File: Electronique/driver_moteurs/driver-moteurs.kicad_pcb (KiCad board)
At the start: 2 copper layers, 51 parts, among them P1 CONN_ENCODER, P2 CONN_02_FREE, P3 CONN_I2C, P4 CONN_Servo, P5 CONN_FC, P6 CONN_SERIAL, P7 CONN_SWDIO, P8 CONN_CAN, U1 stm32f303k8t6, U10 Trou-3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

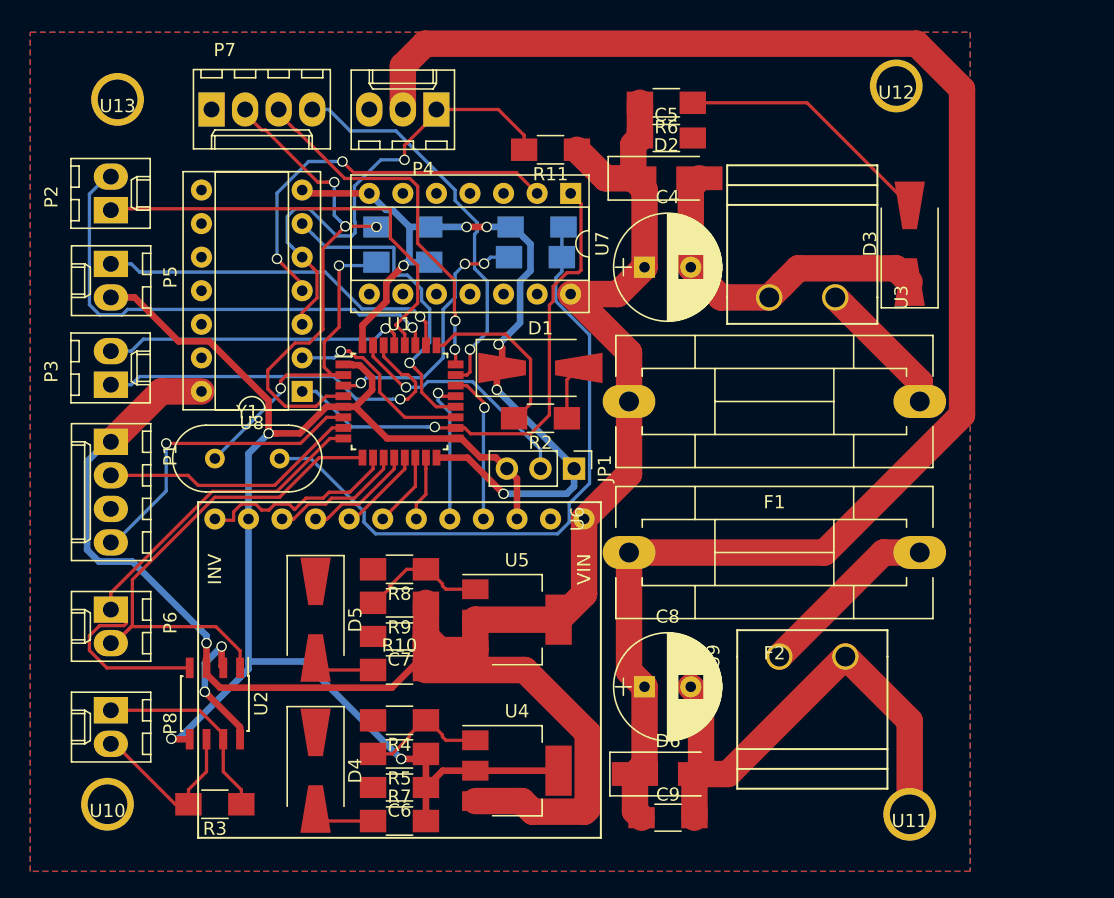
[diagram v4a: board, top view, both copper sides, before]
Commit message: Correction PCB driver moteurs
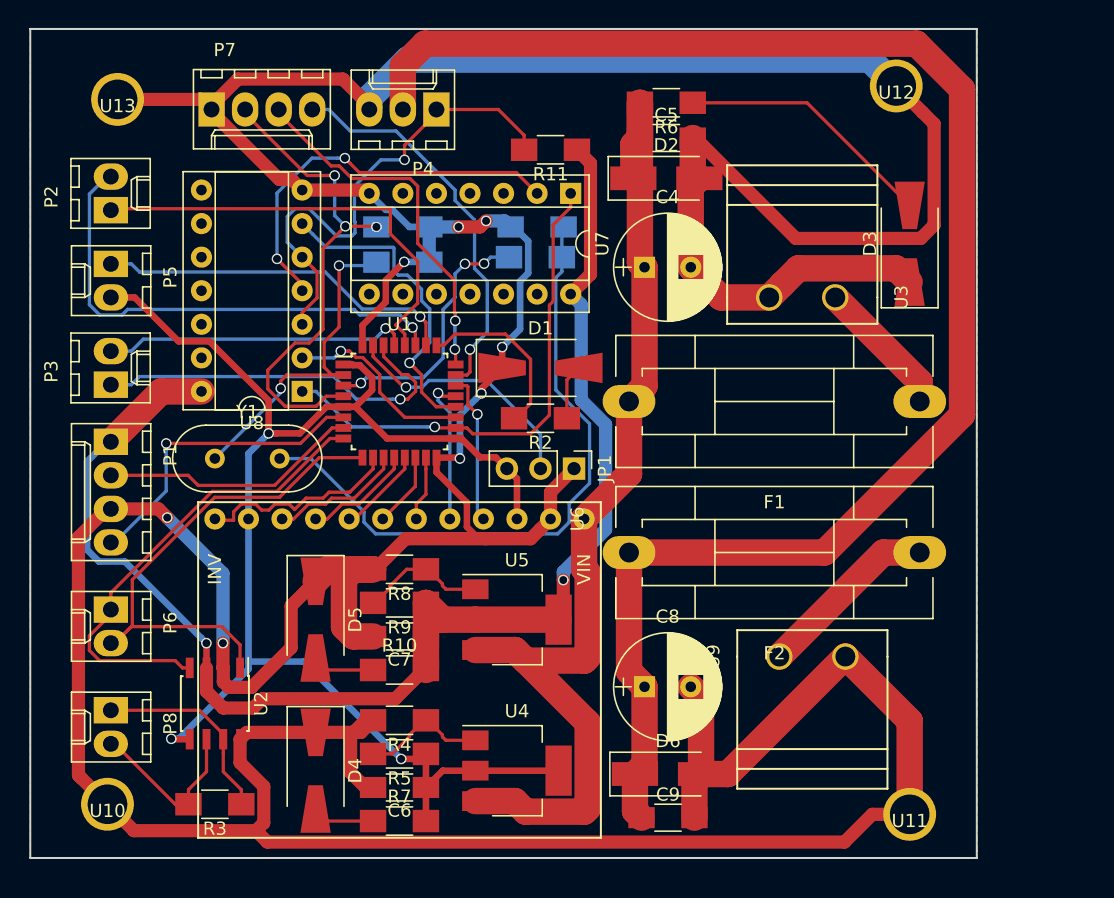
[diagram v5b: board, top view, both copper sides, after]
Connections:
- C4 pad 1: +5V -> VDD
- C5 pad 1: +5V -> VDD
- D2 pad 1: +5V -> VDD
- F1 pad 2: +5V -> VDD
- R6 pad 2: +5V -> VDD
- U4 pad 3: +5V -> VDD
- U5 pad 3: +5V -> VDD
- U6 pad 1: +5V -> VDD
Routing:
- net GND: track 140.7 -> 414.3 mm
- net VDD: track 0.00 -> 82.2 mm
- net +5V: track 151.5 -> 106.8 mm, vias 1 -> 2
- net /TX: track 38.2 -> 35.6 mm
- net /EN_Servo: track 39.2 -> 38.1 mm
- net Net-(JP1-Pad2): track 18.2 -> 19.0 mm
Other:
- board outline added: 71.6 x 62.7 mm

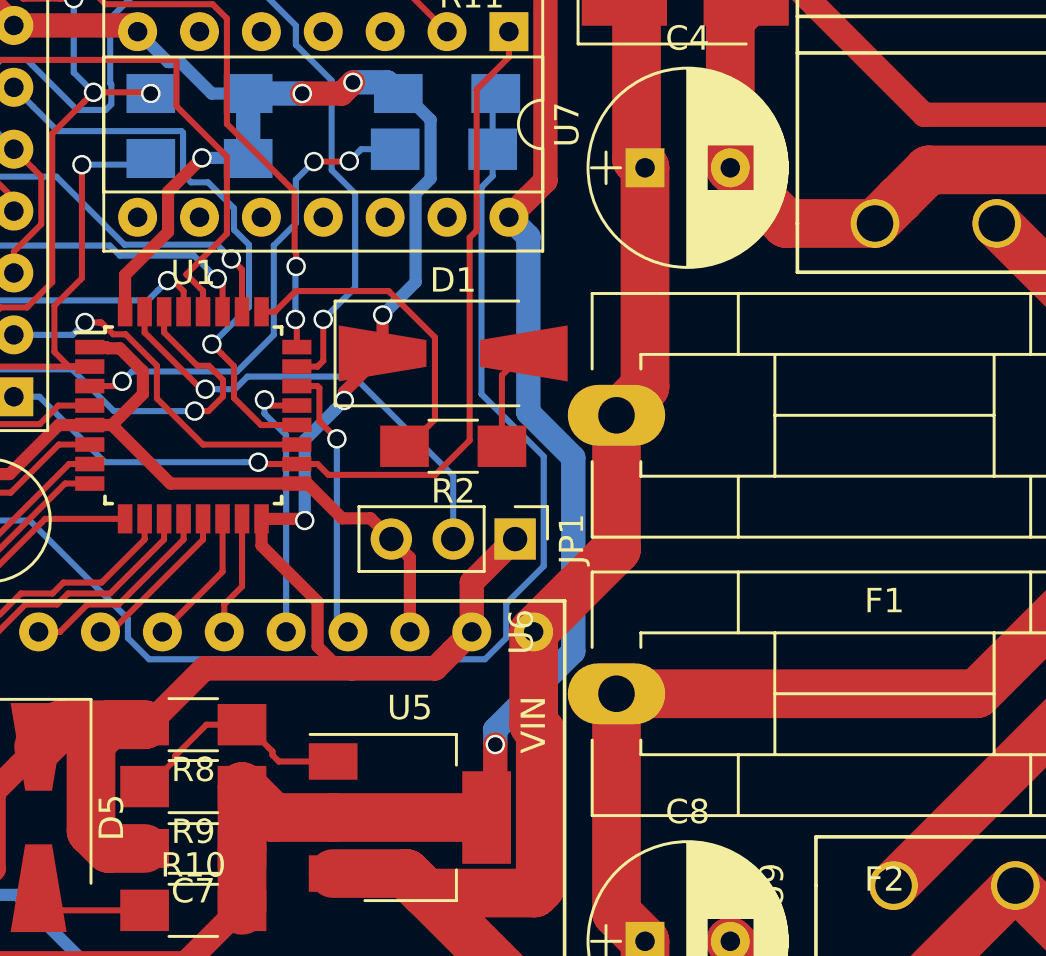
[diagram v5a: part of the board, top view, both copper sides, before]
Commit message: GND driver moteur
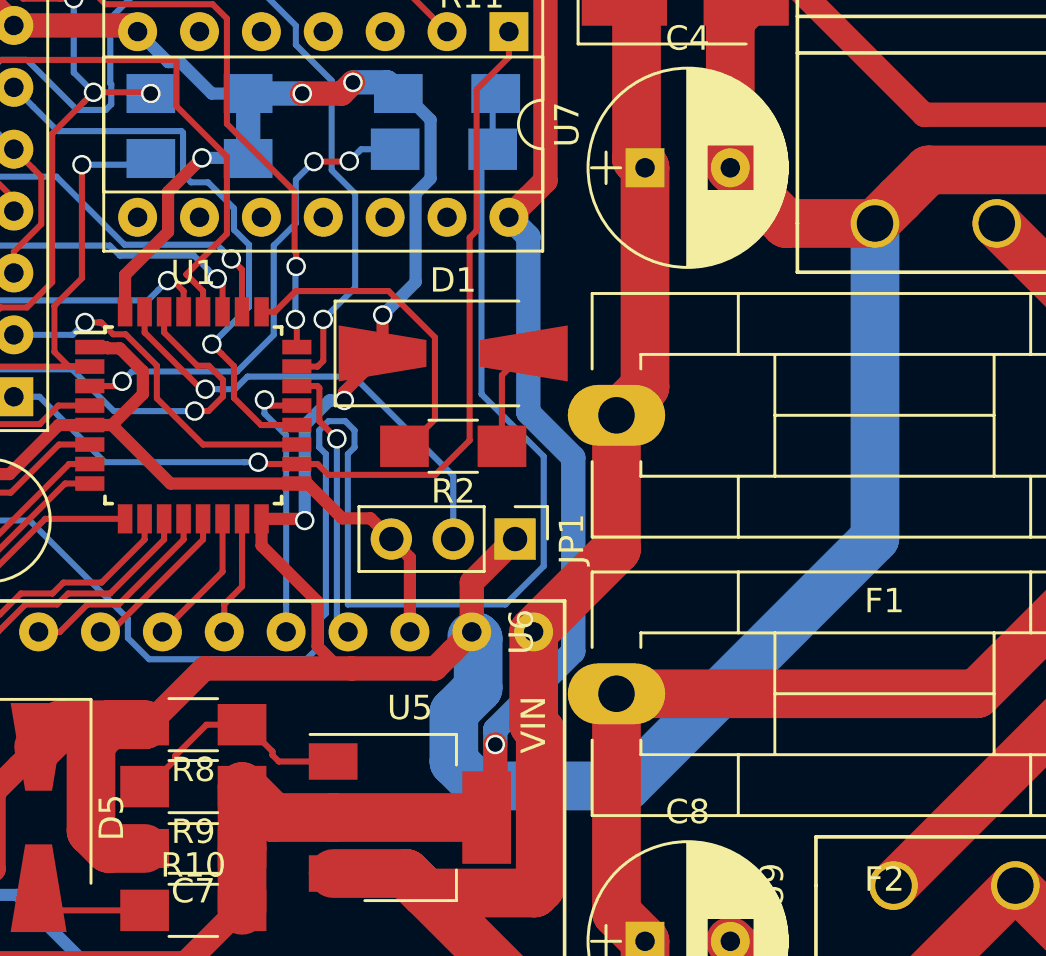
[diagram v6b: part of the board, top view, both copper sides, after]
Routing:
- net GND: track 414.3 -> 455.5 mm
- net Net-(C2-Pad1): track 49.4 -> 64.8 mm
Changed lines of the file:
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@@
     (links 117)
     (no_connects 0)
-    (area 0 0 0 0)
+    (area 92.634999 70.783998 164.420012 133.785)
     (thickness 1.6)
     (drawings 5)
-    (tracks 655)
+    (tracks 676)
     (zones 0)
     (modules 51)
@@
   )
   (setup
-    (last_trace_width 0.25)
+    (last_trace_width 2)
     (user_trace_width 0.25)
     (user_trace_width 0.5)
@@
   (segment (start 111.662629 97.502435) (end 111.662629 98.06812) (width 0.25) (layer F.Cu) (net 1))
   (via (at 111.662629 98.06812) (size 0.8) (drill 0.6) (layers F.Cu B.Cu) (net 1))
-  (segment (start 126.447601 98.850399) (end 126.8476 98.4504) (width 0.5) (layer B.Cu) (net 2))
-  (segment (start 125.222 100.076) (end 126.447601 98.850399) (width 0.5) (layer B.Cu) (net 2))
-  (segment (start 125.222 103.378) (end 125.222 100.076) (width 0.5) (layer B.Cu) (net 2))
+  (segment (start 126.281915 98.4504) (end 126.8476 98.4504) (width 0.5) (layer B.Cu) (net 2))
+  (segment (start 126.23141 98.4504) (end 126.281915 98.4504) (width 0.5) (layer B.Cu) (net 2))
+  (segment (start 131.34519 113.276967) (end 131.34519 111.252903) (width 2) (layer B.Cu) (net 2))
+  (segment (start 125.222 99.45981) (end 126.23141 98.4504) (width 0.5) (layer B.Cu) (net 2))
+  (segment (start 125.222 103.378) (end 125.222 99.45981) (width 0.5) (layer B.Cu) (net 2))
+  (segment (start 132.341033 114.27281) (end 131.34519 113.276967) (width 2) (layer B.Cu) (net 2))
+  (segment (start 131.34519 111.252903) (end 132.341033 110.25706) (width 2) (layer B.Cu) (net 2))
+  (segment (start 132.341033 110.25706) (end 132.341033 108.211033) (width 2) (layer B.Cu) (net 2))
+  (segment (start 132.341033 108.211033) (end 132.280009 108.150009) (width 2) (layer B.Cu) (net 2))
+  (segment (start 132.280009 108.150009) (end 132.08 108.150009) (width 2) (layer B.Cu) (net 2))
+  (segment (start 148.63 91.186) (end 148.63 104.094837) (width 2) (layer B.Cu) (net 2))
+  (segment (start 148.63 104.094837) (end 138.452027 114.27281) (width 2) (layer B.Cu) (net 2))
+  (segment (start 138.452027 114.27281) (end 132.341033 114.27281) (width 2) (layer B.Cu) (net 2))
+  (segment (start 132.341033 114.27281) (end 132.165023 114.0968) (width 2) (layer B.Cu) (net 2))
   (segment (start 118.364 76.962) (end 118.364 76.090717) (width 2) (layer B.Cu) (net 2))
   (segment (start 118.364 76.090717) (end 121.270716 73.184001) (width 2) (layer B.Cu) (net 2))
@@
   (segment (start 142.97 130.556) (end 142.97 127.754) (width 2) (layer F.Cu) (net 2))
   (segment (start 142.97 127.754) (end 143.47 127.254) (width 2) (layer F.Cu) (net 2))
-  (segment (start 132.937 89.238) (end 132.937 88.138) (width 0.25) (layer B.Cu) (net 3))
-  (segment (start 132.478999 89.696001) (end 132.937 89.238) (width 0.25) (layer B.Cu) (net 3))
-  (segment (start 133.494999 106.788003) (end 135.033001 105.250001) (width 0.25) (layer B.Cu) (net 3))
+  (segment (start 135.033001 100.747471) (end 132.478999 98.193469) (width 0.25) (layer B.Cu) (net 3))
+  (segment (start 132.478999 88.596001) (end 132.937 88.138) (width 0.25) (layer B.Cu) (net 3))
   (segment (start 135.033001 105.250001) (end 135.033001 100.747471) (width 0.25) (layer B.Cu) (net 3))
-  (segment (start 118.839999 109.075001) (end 132.620001 109.075001) (width 0.25) (layer B.Cu) (net 3))
-  (segment (start 132.620001 109.075001) (end 133.494999 108.200003) (width 0.25) (layer B.Cu) (net 3))
+  (segment (start 118.839999 109.075001) (end 125.289999 109.075001) (width 0.25) (layer B.Cu) (net 3))
+  (segment (start 133.458003 106.824999) (end 135.033001 105.250001) (width 0.25) (layer B.Cu) (net 3))
+  (segment (start 126.09279 100.648192) (end 125.817799 100.373201) (width 0.25) (layer B.Cu) (net 3))
+  (segment (start 126.99281 106.824999) (end 133.458003 106.824999) (width 0.25) (layer B.Cu) (net 3))
+  (segment (start 126.99281 100.648192) (end 126.99281 106.824999) (width 0.25) (layer B.Cu) (net 3))
+  (segment (start 127.267801 99.677199) (end 127.267801 100.373201) (width 0.25) (layer B.Cu) (net 3))
+  (segment (start 125.817799 99.677199) (end 126.194799 99.300199) (width 0.25) (layer B.Cu) (net 3))
+  (segment (start 127.267801 100.373201) (end 126.99281 100.648192) (width 0.25) (layer B.Cu) (net 3))
+  (segment (start 125.817799 100.373201) (end 125.817799 99.677199) (width 0.25) (layer B.Cu) (net 3))
+  (segment (start 126.09279 107.192208) (end 126.09279 100.648192) (width 0.25) (layer B.Cu) (net 3))
+  (segment (start 126.890801 99.300199) (end 127.267801 99.677199) (width 0.25) (layer B.Cu) (net 3))
+  (segment (start 125.874999 107.409999) (end 126.09279 107.192208) (width 0.25) (layer B.Cu) (net 3))
+  (segment (start 132.478999 98.193469) (end 132.478999 88.596001) (width 0.25) (layer B.Cu) (net 3))
+  (segment (start 125.874999 108.490001) (end 125.874999 107.409999) (width 0.25) (layer B.Cu) (net 3))
+  (segment (start 125.289999 109.075001) (end 125.874999 108.490001) (width 0.25) (layer B.Cu) (net 3))
   (segment (start 117.965001 108.200003) (end 118.839999 109.075001) (width 0.25) (layer B.Cu) (net 3))
   (segment (start 117.965001 107.409999) (end 117.965001 108.200003) (width 0.25) (layer B.Cu) (net 3))
+  (segment (start 126.194799 99.300199) (end 126.890801 99.300199) (width 0.25) (layer B.Cu) (net 3))
   (segment (start 113.933002 103.378) (end 117.965001 107.409999) (width 0.25) (layer B.Cu) (net 3))
   (segment (start 111.58 103.378) (end 113.933002 103.378) (width 0.25) (layer B.Cu) (net 3))
-  (segment (start 132.478999 98.193469) (end 132.478999 89.696001) (width 0.25) (layer B.Cu) (net 3))
-  (segment (start 135.033001 100.747471) (end 132.478999 98.193469) (width 0.25) (layer B.Cu) (net 3))
-  (segment (start 133.494999 108.200003) (end 133.494999 106.788003) (width 0.25) (layer B.Cu) (net 3))
   (segment (start 132.937 88.138) (end 132.937 85.979) (width 0.25) (layer B.Cu) (net 3))
   (segment (start 132.937 85.979) (end 133.064 85.852) (width 0.25) (layer B.Cu) (net 3))

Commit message: ecritures
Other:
- board text added: "+18V"
- board text added: "CAN"
- board text added: "Encodeur"
- board text added: "Fc"
- board text added: "I2C"
- board text added: "Libre"
- board text added: "ST-Link"
- board text added: "Serial"
- board text added: "Servo"
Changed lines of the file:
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@@
-(kicad_pcb (version 4) (host pcbnew 4.0.7)
+(kicad_pcb (version 4) (host pcbnew 4.0.2+dfsg1-stable)
   (general
     (links 117)
     (no_connects 0)
-    (area 92.634999 70.783998 164.420012 133.785)
+    (area 92.634999 70.783998 164.420012 133.685)
     (thickness 1.6)
-    (drawings 5)
+    (drawings 15)
     (tracks 676)
     (zones 0)
@@
   )
   (setup
-    (last_trace_width 2)
+    (last_trace_width 0.25)
     (user_trace_width 0.25)
     (user_trace_width 0.5)
@@
       (effects (font (size 1 1) (thickness 0.15)))
     )
-    (fp_text value CONN_CAN (at 1.27 4.5 270) (layer F.Fab)
+    (fp_text value CONN_CAN (at 3.772 -3.254 270) (layer F.Fab)
       (effects (font (size 1 1) (thickness 0.15)))
     )
@@
       (effects (font (size 1 1) (thickness 0.15)))
     )
-    (fp_text value CONN_SERIAL (at 1.27 4.5 270) (layer F.Fab)
+    (fp_text value CONN_SERIAL (at 0.442 -4.704 270) (layer F.Fab)
       (effects (font (size 1 1) (thickness 0.15)))
     )
@@
       (effects (font (size 1 1) (thickness 0.15)))
     )
-    (fp_text value CONN_ENCODER (at 3.81 4.5 270) (layer F.Fab)
+    (fp_text value CONN_ENCODER (at 3.772 -3.334 270) (layer F.Fab)
       (effects (font (size 1 1) (thickness 0.15)))
     )
@@
     (descr "Connector Headers with Friction Lock, 22-27-2041, http://www.molex.com/pdm_docs/sd/022272021_sd.pdf")
     (tags "connector molex kk_6410 22-27-2041")
-    (fp_text reference P7 (at 1 -4.5) (layer F.SilkS)
+    (fp_text reference P7 (at -2.906 -2.272) (layer F.SilkS)
       (effects (font (size 1 1) (thickness 0.15)))
     )
@@
       (effects (font (size 1 1) (thickness 0.15)))
     )
-    (fp_text value CONN_Servo (at 2.54 4.5 180) (layer F.Fab)
+    (fp_text value CONN_Servo (at 1.294 -2.968 180) (layer F.Fab)
       (effects (font (size 1 1) (thickness 0.15)))
     )
@@
       (effects (font (size 1 1) (thickness 0.15)))
     )
-    (fp_text value CONN_FC (at 1.27 4.5 270) (layer F.Fab)
+    (fp_text value CONN_FC (at 1.324 -4.164 270) (layer F.Fab)
       (effects (font (size 1 1) (thickness 0.15)))
     )
@@
     (descr "Connector Headers with Friction Lock, 22-27-2021, http://www.molex.com/pdm_docs/sd/022272021_sd.pdf")
     (tags "connector molex kk_6410 22-27-2021")
-    (fp_text reference P3 (at 1 -4.5 90) (layer F.SilkS)
+    (fp_text reference P3 (at 1.7 2.514 90) (layer F.SilkS)
       (effects (font (size 1 1) (thickness 0.15)))
     )
@@
     (descr "Connector Headers with Friction Lock, 22-27-2021, http://www.molex.com/pdm_docs/sd/022272021_sd.pdf")
     (tags "connector molex kk_6410 22-27-2021")
-    (fp_text reference P2 (at 1 -4.5 90) (layer F.SilkS)
+    (fp_text reference P2 (at 1.562 2.774 90) (layer F.SilkS)
       (effects (font (size 1 1) (thickness 0.15)))
     )
@@
     )
   )
+  (gr_text Servo (at 152.18 129.87) (layer F.SilkS)
+    (effects (font (size 1.5 1.5) (thickness 0.3)))
+  )
+  (gr_text +18V (at 150.44 78.85) (layer F.SilkS)
+    (effects (font (size 1.5 1.5) (thickness 0.3)))
+  )
+  (gr_text CAN (at 94.17 123.6 90) (layer F.SilkS)
+    (effects (font (size 1.5 1.5) (thickness 0.3)))
+  )
+  (gr_text Serial (at 93.97 116.41 90) (layer F.SilkS)
+    (effects (font (size 1.5 1.5) (thickness 0.3)))
+  )
+  (gr_text Encodeur (at 94.01 106.12 90) (layer F.SilkS)
+    (effects (font (size 1.5 1.5) (thickness 0.3)))
+  )
+  (gr_text I2C (at 94.17 96.37 90) (layer F.SilkS)
+    (effects (font (size 1.5 1.5) (thickness 0.3)))
+  )
+  (gr_text Fc (at 94.13 89.72 90) (layer F.SilkS)
+    (effects (font (size 1.5 1.5) (thickness 0.3)))
+  )
+  (gr_text Libre (at 94.1 82.86 90) (layer F.SilkS)
+    (effects (font (size 1.5 1.5) (thickness 0.3)))
+  )
+  (gr_text Servo (at 120.8 72.34) (layer F.SilkS)
+    (effects (font (size 1.5 1.5) (thickness 0.3)))
+  )
+  (gr_text ST-Link (at 110.42 72.23) (layer F.SilkS)
+    (effects (font (size 1.5 1.5) (thickness 0.3)))
+  )
   (gr_line (start 92.71 133.604) (end 92.71 70.866) (angle 90) (layer Edge.Cuts) (width 0.15))
